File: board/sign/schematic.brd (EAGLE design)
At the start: 97.8 x 65.8 mm, 37 parts, among them IC1 STM32F207ZGT, IC3 LM3940, J1 DCJ0202, J2 2908-05WB-MG, X2 22-23-2041

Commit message: Final board
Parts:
- removed J2: 2908-05WB-MG, 2908-05WB-MG:3M_2908-05WB-MG
- added J3: DM3AT-SF-PEJM5, connector:DM3AT-SF-PEJM5
- added R5: 470, rcl:0204/7
- added S2: (no value), switch-omron:B3F-10XX
- C19: device rcl:C025-025X050 -> rcl:E2,5-6
- C2, C23: device rcl:C025-025X050 -> rcl:C050-024X044
- C4, C5: device rcl:C025-025X050 -> rcl:E1,8-4
- moved C21 11.4 mm to (86.4, 17.9)
- moved R2 5.08 mm to (90.2, 28.1)
- moved R3 4.97 mm to (95.1, 30.9)
- moved C2 0.76 mm to (55.3, 20.6)
- moved C19 0.63 mm to (67.7, 24.9)
- moved C5 0.52 mm to (39.0, 51.4), turned to 90 degrees
- turned C4 to 90 degrees
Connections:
- removed net N$4: IC2.12, R3.2
- new net FLASH: IC2.12, R3.2, R5.2
- new net N$1: R5.1, S2.1, S2.2
- net +3V3: now also C19.+, J3.4; no longer C19.1, J2.4
- net GND: now also C19.-, C4.-, C5.-, J3.6, J3.MOUNT0, J3.MOUNT1, J3.MOUNT2, J3.MOUNT3, S2.3, S2.4; no longer C19.2, C4.1, C5.1, J2.6
- net MISO: now also J3.7; no longer J2.7
- net MOSI: now also J3.3; no longer J2.3
- net N$2: now also C5.+; no longer C5.2
- net N$3: now also C4.+; no longer C4.2
- net SCLK: now also J3.5; no longer J2.5
- net SDCS: now also J3.2; no longer J2.2
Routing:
- net FLASH: track 0.00 -> 55.5 mm
- net SDCS: track 35.7 -> 21.8 mm
- net MISO: track 27.3 -> 13.5 mm
- net MOSI: track 42.5 -> 28.9 mm
- net SCLK: track 29.6 -> 16.7 mm
- net N$1: track 0.00 -> 12.4 mm
- net +3V3: track 85.7 -> 73.8 mm
- net DEBUG_TX: track 36.9 -> 31.6 mm
- net RX: track 65.6 -> 60.5 mm
- net N$4: track 3.01 -> 0.00 mm
- net +5V: track 40.5 -> 39.3 mm
- net ESP_PROG_RX: track 29.5 -> 30.1 mm
- net ESP_PROG_TX: track 24.7 -> 25.3 mm
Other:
- board text added: "2"
- board text added: "FLASH"
- board text added: "For HUB75 compatible displays. Designed in Canada"
- board text added: "M"

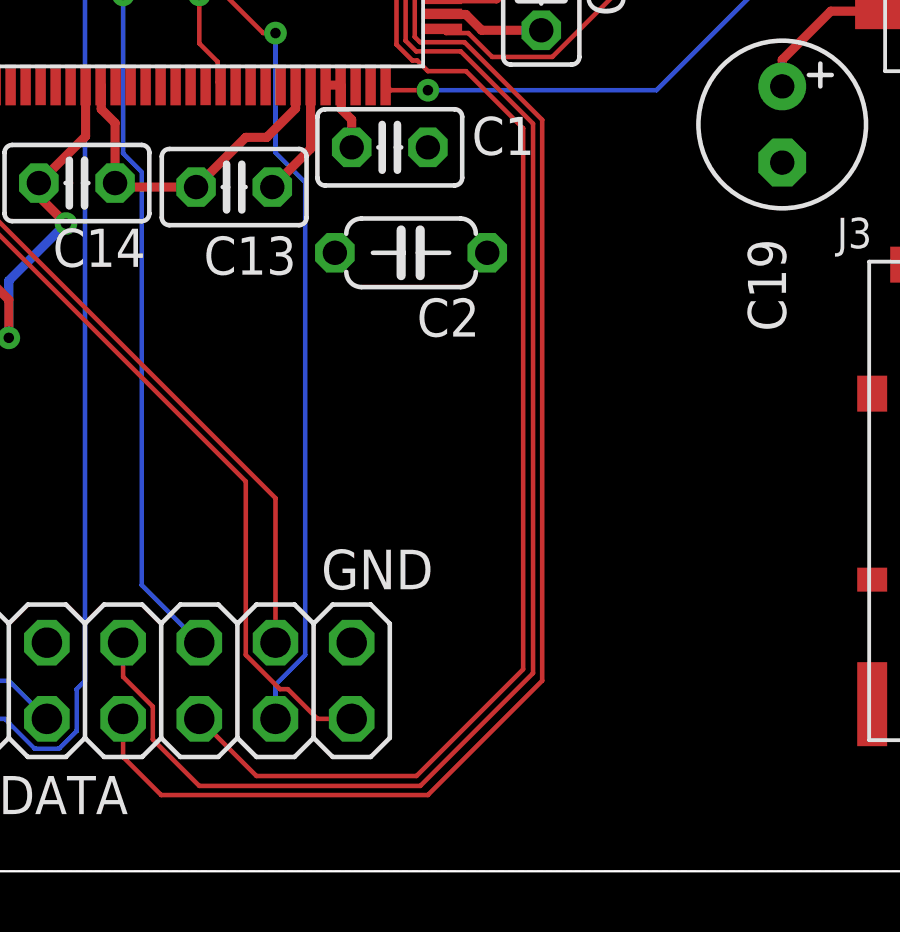
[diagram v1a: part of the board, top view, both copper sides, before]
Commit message: Add noise-cleanup cap
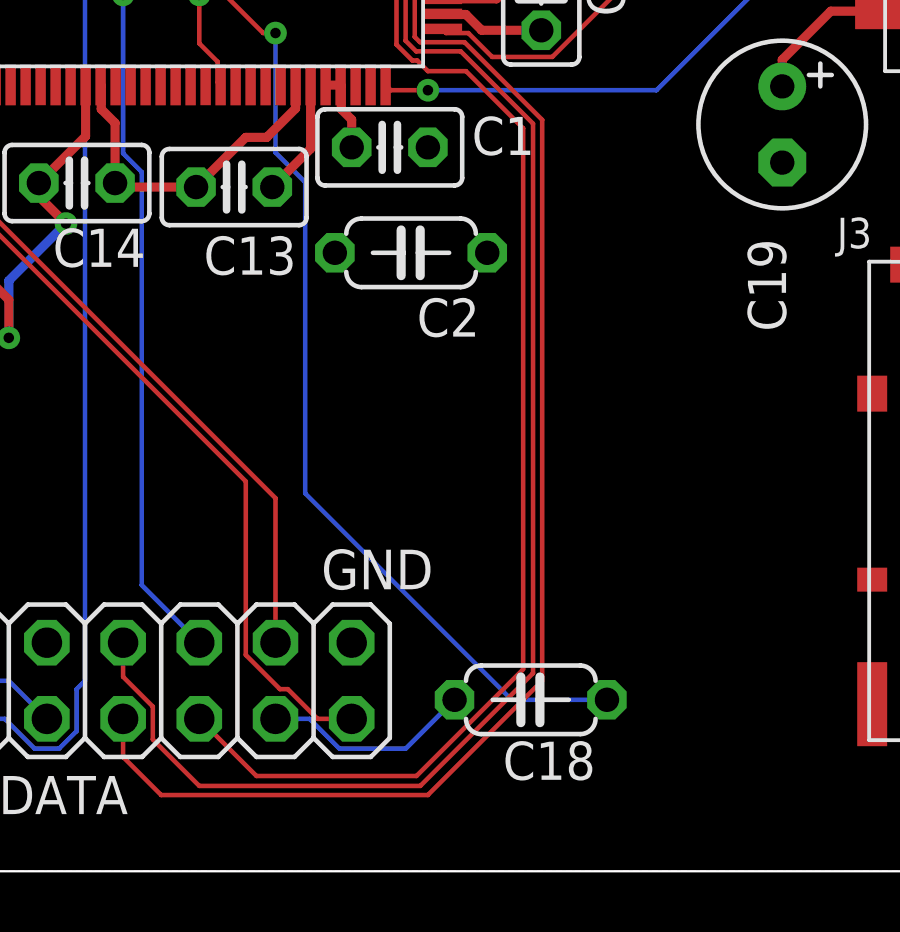
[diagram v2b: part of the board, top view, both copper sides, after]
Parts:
- added C18: 10pF, rcl:C050-024X044
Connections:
- new net N$4: C18.2, JP1.13
- net DCLK: now also C18.1; no longer JP1.13
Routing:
- net N$4: track 0.00 -> 7.05 mm
- net DCLK: track 44.0 -> 49.0 mm
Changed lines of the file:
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@@
 <attribute name="NAME" x="70.098" y="20.766" size="1.016" layer="25" font="vector" ratio="12" align="bottom-center"/>
+</element>
+<element name="C18" library="rcl" library_urn="urn:adsk.eagle:library:334" package="C050-024X044" package3d_urn="urn:adsk.eagle:package:23643/1" value="10pF" x="59.309" y="5.715" smashed="yes" rot="R180">
+<attribute name="NAME" x="61.468" y="4.318" size="1.27" layer="25" ratio="10" rot="R180"/>
+<attribute name="SPICEPREFIX" value="C" x="59.309" y="5.715" size="1.778" layer="27" rot="R180" display="off"/>
+<attribute name="VALUE" x="61.468" y="8.382" size="1.27" layer="27" ratio="10" rot="R180"/>
 </element>
 </elements>
@@
 <signal name="DCLK">
 <contactref element="IC1" pad="122"/>
-<contactref element="JP1" pad="13"/>
 <via x="50.8" y="27.94" extent="1-16" drill="0.35"/>
 <wire x1="50.8" y1="27.94" x2="50.8" y2="23.9563875" width="0.1524" layer="16"/>
-<wire x1="50.8" y1="6.219075" x2="50.8" y2="5.08" width="0.1524" layer="16"/>
-<wire x1="51.7906" y1="7.209675" x2="50.8" y2="6.219075" width="0.1524" layer="16"/>
 <wire x1="50.8" y1="23.9563875" x2="51.7906" y2="22.9657875" width="0.1524" layer="16"/>
-<wire x1="51.7906" y1="22.9657875" x2="51.7906" y2="7.209675" width="0.1524" layer="16"/>
 <wire x1="35.095" y1="39.08" x2="35.1914" y2="38.9836" width="0.1524" layer="1"/>
 <wire x1="35.1914" y1="38.9836" x2="35.8646875" y2="38.9836" width="0.1524" layer="1"/>
@@
 <wire x1="35.8646875" y1="38.9836" x2="45.0314875" y2="29.8168" width="0.1524" layer="1"/>
 <wire x1="45.0314875" y1="29.8168" x2="48.51135" y2="29.8168" width="0.1524" layer="1"/>
+<contactref element="C18" pad="1"/>
+<wire x1="51.7906" y1="22.9657875" x2="51.7906" y2="12.5984" width="0.1524" layer="16"/>
+<wire x1="61.849" y1="5.715" x2="58.674" y2="5.715" width="0.1524" layer="16"/>
+<wire x1="58.674" y1="5.715" x2="51.7906" y2="12.5984" width="0.1524" layer="16"/>
 </signal>
 <signal name="A">
@@
 <wire x1="37.97" y1="49.480915625" x2="39.000071875" y2="50.5109875" width="0.3048" layer="1"/>
 </signal>
+<signal name="N$4">
+<contactref element="JP1" pad="13"/>
+<contactref element="C18" pad="2"/>
+<wire x1="51.939075" y1="5.08" x2="50.8" y2="5.08" width="0.1524" layer="16"/>
+<wire x1="52.929675" y1="4.0894" x2="51.939075" y2="5.08" width="0.1524" layer="16"/>
+<wire x1="55.1434" y1="4.0894" x2="52.929675" y2="4.0894" width="0.1524" layer="16"/>
+<wire x1="56.769" y1="5.715" x2="55.1434" y2="4.0894" width="0.1524" layer="16"/>
+</signal>
 </signals>

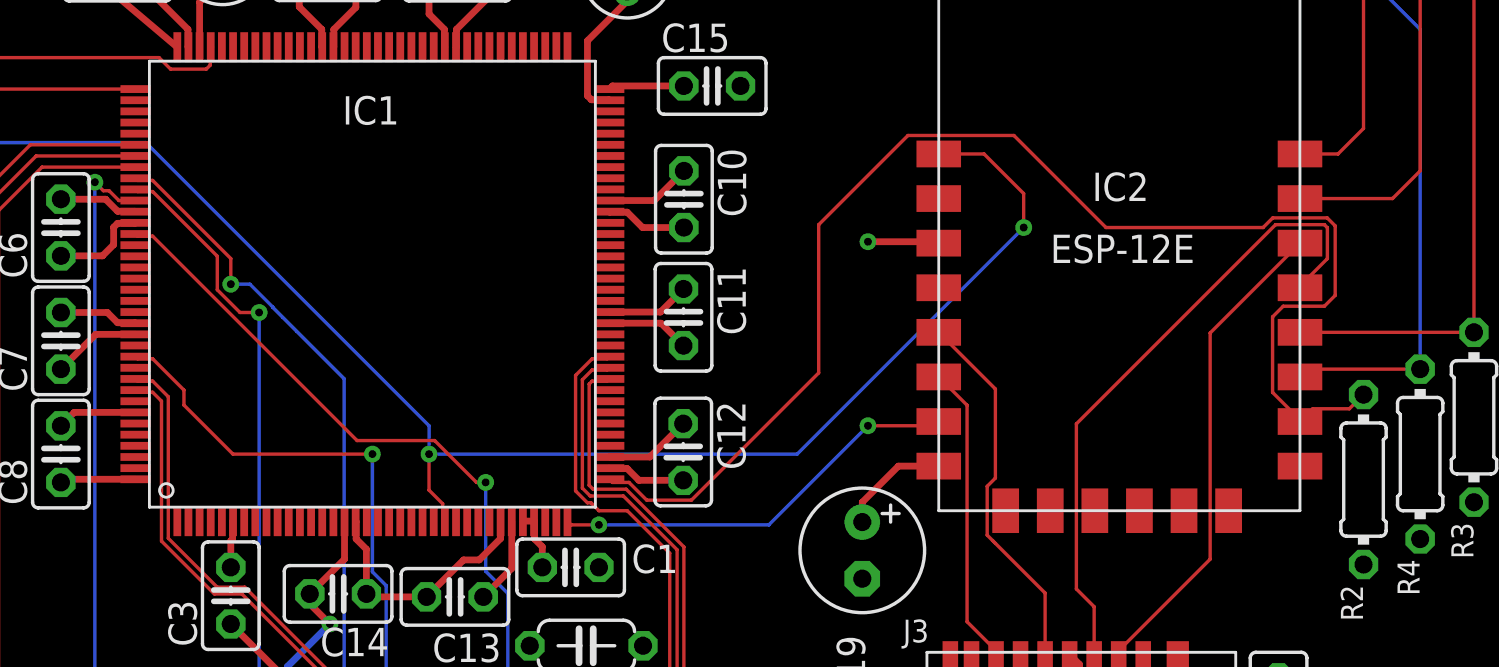
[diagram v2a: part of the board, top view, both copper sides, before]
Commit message: Fix board again -- god damned incorrect docs
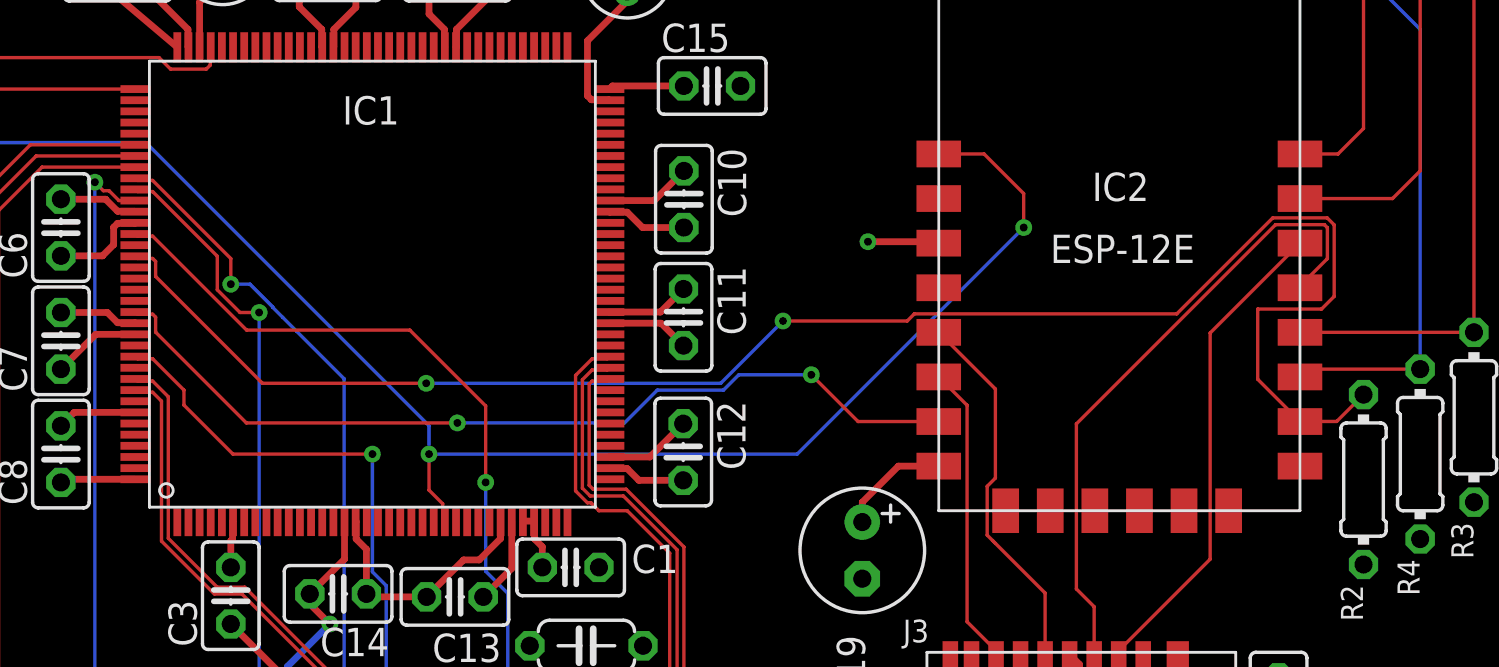
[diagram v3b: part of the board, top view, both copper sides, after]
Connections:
- net RX: now also IC1.124; no longer IC1.37
- net TX: now also IC1.129; no longer IC1.36
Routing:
- net TX: track 18.6 -> 40.2 mm
- net RX: track 60.5 -> 75.8 mm, vias 0 -> 2
- net DCLK: track 49.0 -> 51.0 mm
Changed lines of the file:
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@@
 <wire x1="35.095" y1="39.08" x2="35.1914" y2="38.9836" width="0.1524" layer="1"/>
 <wire x1="35.1914" y1="38.9836" x2="35.8646875" y2="38.9836" width="0.1524" layer="1"/>
-<wire x1="50.38815" y1="27.94" x2="50.8" y2="27.94" width="0.1524" layer="1"/>
-<wire x1="48.51135" y1="29.8168" x2="50.38815" y2="27.94" width="0.1524" layer="1"/>
-<wire x1="35.8646875" y1="38.9836" x2="45.0314875" y2="29.8168" width="0.1524" layer="1"/>
-<wire x1="45.0314875" y1="29.8168" x2="48.51135" y2="29.8168" width="0.1524" layer="1"/>
+<wire x1="35.8646875" y1="38.9836" x2="40.0784875" y2="34.7698" width="0.1524" layer="1"/>
 <contactref element="C18" pad="1"/>
 <wire x1="51.7906" y1="22.9657875" x2="51.7906" y2="12.5984" width="0.1524" layer="16"/>
 <wire x1="61.849" y1="5.715" x2="58.674" y2="5.715" width="0.1524" layer="16"/>
 <wire x1="58.674" y1="5.715" x2="51.7906" y2="12.5984" width="0.1524" layer="16"/>
+<wire x1="47.3992" y1="34.7698" x2="50.8" y2="31.369" width="0.1524" layer="1"/>
+<wire x1="50.8" y1="31.369" x2="50.8" y2="27.94" width="0.1524" layer="1"/>
+<wire x1="40.0784875" y1="34.7698" x2="47.3992" y2="34.7698" width="0.1524" layer="1"/>
 </signal>
 <signal name="A">
@@
 </signal>
 <signal name="TX">
-<contactref element="IC1" pad="36"/>
 <contactref element="IC2" pad="7"/>
-<via x="67.945" y="30.48" extent="1-16" drill="0.35"/>
-<via x="55.88" y="26.035" extent="1-16" drill="0.35"/>
-<wire x1="54.47" y1="26.205" x2="54.64" y2="26.035" width="0.1524" layer="1"/>
-<wire x1="54.64" y1="26.035" x2="55.88" y2="26.035" width="0.1524" layer="1"/>
-<wire x1="67.945" y1="30.48" x2="70.93" y2="30.48" width="0.1524" layer="1"/>
-<wire x1="70.93" y1="30.48" x2="71.12" y2="30.67" width="0.1524" layer="1"/>
-<wire x1="55.88" y1="26.035" x2="63.5" y2="26.035" width="0.1524" layer="16"/>
-<wire x1="63.5" y1="26.035" x2="67.945" y2="30.48" width="0.1524" layer="16"/>
+<contactref element="IC1" pad="129"/>
+<via x="65.405" y="32.766" extent="1-16" drill="0.35"/>
+<via x="49.53" y="30.607" extent="1-16" drill="0.35"/>
+<wire x1="40.068" y1="30.607" x2="49.53" y2="30.607" width="0.1524" layer="1"/>
+<wire x1="35.095" y1="35.58" x2="35.1914" y2="35.4836" width="0.1524" layer="1"/>
+<wire x1="35.1914" y1="35.4836" x2="35.8646875" y2="35.4836" width="0.1524" layer="1"/>
+<wire x1="35.8646875" y1="35.4836" x2="35.9986" y2="35.3496875" width="0.1524" layer="1"/>
+<wire x1="35.9986" y1="34.6764" x2="40.068" y2="30.607" width="0.1524" layer="1"/>
+<wire x1="35.9986" y1="35.3496875" x2="35.9986" y2="34.6764" width="0.1524" layer="1"/>
+<wire x1="65.405" y1="32.766" x2="67.501" y2="30.67" width="0.1524" layer="1"/>
+<wire x1="67.501" y1="30.67" x2="71.12" y2="30.67" width="0.1524" layer="1"/>
+<wire x1="49.53" y1="30.607" x2="57.023" y2="30.607" width="0.1524" layer="16"/>
+<wire x1="58.4962" y1="32.0802" x2="61.46725625" y2="32.0802" width="0.1524" layer="16"/>
+<wire x1="62.15305625" y1="32.766" x2="65.405" y2="32.766" width="0.1524" layer="16"/>
+<wire x1="61.46725625" y1="32.0802" x2="62.15305625" y2="32.766" width="0.1524" layer="16"/>
+<wire x1="57.023" y1="30.607" x2="58.4962" y2="32.0802" width="0.1524" layer="16"/>
 </signal>
 <signal name="RX">
-<contactref element="IC1" pad="37"/>
 <contactref element="IC2" pad="10"/>
 <contactref element="R2" pad="2"/>
-<wire x1="69.73754375" y1="43.4986" x2="65.7352" y2="39.49625625" width="0.1524" layer="1"/>
-<wire x1="60.027215625" y1="27.144084375" x2="58.023146875" y2="27.144084375" width="0.1524" layer="1"/>
-<wire x1="58.023146875" y1="27.144084375" x2="57.22723125" y2="27.94" width="0.1524" layer="1"/>
-<wire x1="65.7352" y1="39.49625625" x2="65.7352" y2="32.85206875" width="0.1524" layer="1"/>
-<wire x1="65.7352" y1="32.85206875" x2="60.027215625" y2="27.144084375" width="0.1524" layer="1"/>
-<wire x1="74.4914" y1="43.4986" x2="69.73754375" y2="43.4986" width="0.1524" layer="1"/>
-<wire x1="56.485" y1="27.94" x2="56.345" y2="28.08" width="0.1524" layer="1"/>
-<wire x1="57.22723125" y1="27.94" x2="56.485" y2="27.94" width="0.1524" layer="1"/>
-<wire x1="90.17" y1="31.877" x2="89.535" y2="31.242" width="0.1524" layer="1"/>
-<wire x1="89.535" y1="31.242" x2="87.892" y2="31.242" width="0.1524" layer="1"/>
-<wire x1="87.32" y1="30.67" x2="87.892" y2="31.242" width="0.1524" layer="1"/>
-<wire x1="86.0914" y1="35.3646875" x2="86.5681125" y2="35.8414" width="0.1524" layer="1"/>
-<wire x1="87.32" y1="30.67" x2="87.32" y2="30.7467125" width="0.1524" layer="1"/>
-<wire x1="87.32" y1="30.7467125" x2="86.0914" y2="31.9753125" width="0.1524" layer="1"/>
-<wire x1="86.0914" y1="31.9753125" x2="86.0914" y2="35.3646875" width="0.1524" layer="1"/>
-<wire x1="86.5681125" y1="35.8414" x2="88.4146875" y2="35.8414" width="0.1524" layer="1"/>
-<wire x1="88.4146875" y1="35.8414" x2="88.9" y2="36.3267125" width="0.1524" layer="1"/>
-<wire x1="78.62" y1="39.37" x2="74.4914" y2="43.4986" width="0.1524" layer="1"/>
-<wire x1="85.66565625" y1="39.37" x2="78.62" y2="39.37" width="0.1524" layer="1"/>
-<wire x1="88.54094375" y1="39.8034" x2="86.09905625" y2="39.8034" width="0.1524" layer="1"/>
-<wire x1="86.09905625" y1="39.8034" x2="85.66565625" y2="39.37" width="0.1524" layer="1"/>
-<wire x1="88.9" y1="39.44434375" x2="88.54094375" y2="39.8034" width="0.1524" layer="1"/>
-<wire x1="88.9" y1="36.3267125" x2="88.9" y2="39.44434375" width="0.1524" layer="1"/>
+<contactref element="IC1" pad="124"/>
+<via x="48.133" y="32.385" extent="1-16" drill="0.35"/>
+<via x="64.135" y="35.179" extent="1-16" drill="0.35"/>
+<wire x1="40.79" y1="32.385" x2="48.133" y2="32.385" width="0.1524" layer="1"/>
+<wire x1="35.095" y1="38.08" x2="35.1914" y2="37.9836" width="0.1524" layer="1"/>
+<wire x1="35.1914" y1="37.9836" x2="35.8646875" y2="37.9836" width="0.1524" layer="1"/>
+<wire x1="35.8646875" y1="37.9836" x2="35.9986" y2="37.8496875" width="0.1524" layer="1"/>
+<wire x1="35.9986" y1="37.1764" x2="40.79" y2="32.385" width="0.1524" layer="1"/>
+<wire x1="35.9986" y1="37.8496875" x2="35.9986" y2="37.1764" width="0.1524" layer="1"/>
+<wire x1="86.09905625" y1="39.8034" x2="88.54094375" y2="39.8034" width="0.1524" layer="1"/>
+<wire x1="88.54094375" y1="39.8034" x2="88.8534" y2="39.49094375" width="0.1524" layer="1"/>
+<wire x1="64.135" y1="35.179" x2="69.7057125" y2="35.179" width="0.1524" layer="1"/>
+<wire x1="69.7057125" y1="35.179" x2="70.0253125" y2="35.4986" width="0.1524" layer="1"/>
+<wire x1="81.79425625" y1="35.4986" x2="86.09905625" y2="39.8034" width="0.1524" layer="1"/>
+<wire x1="88.2876875" y1="35.7144" x2="85.4248" y2="35.7144" width="0.1524" layer="1"/>
+<wire x1="70.0253125" y1="35.4986" x2="81.79425625" y2="35.4986" width="0.1524" layer="1"/>
+<wire x1="88.8534" y1="39.49094375" x2="88.8534" y2="36.2801125" width="0.1524" layer="1"/>
+<wire x1="88.8534" y1="36.2801125" x2="88.2876875" y2="35.7144" width="0.1524" layer="1"/>
+<wire x1="85.4248" y1="35.7144" x2="85.4248" y2="32.5652" width="0.1524" layer="1"/>
+<wire x1="85.4248" y1="32.5652" x2="87.316" y2="30.674" width="0.1524" layer="1"/>
+<wire x1="87.316" y1="30.674" x2="87.32" y2="30.67" width="0.1524" layer="1"/>
+<wire x1="48.133" y1="32.385" x2="61.341" y2="32.385" width="0.1524" layer="16"/>
+<wire x1="61.341" y1="32.385" x2="64.135" y2="35.179" width="0.1524" layer="16"/>
+<wire x1="90.17" y1="31.877" x2="88.967" y2="30.674" width="0.1524" layer="1"/>
+<wire x1="88.967" y1="30.674" x2="87.316" y2="30.674" width="0.1524" layer="1"/>
 </signal>
 <signal name="SCLK">
